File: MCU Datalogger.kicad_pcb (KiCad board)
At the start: 2 copper layers, 51.4 x 34.3 mm, 31 parts, among them J1 Conn_01x04_Male, J2 Conn_01x09_Male, J3 Conn_01x04_Male, J4 Conn_02x03_Odd_Even, U1 24LC1025, U2 DS1337S+, U3 24LC1025, U4 ATMEGA328P-AU, Y1 32.768 KHz, Y2 16 MHz

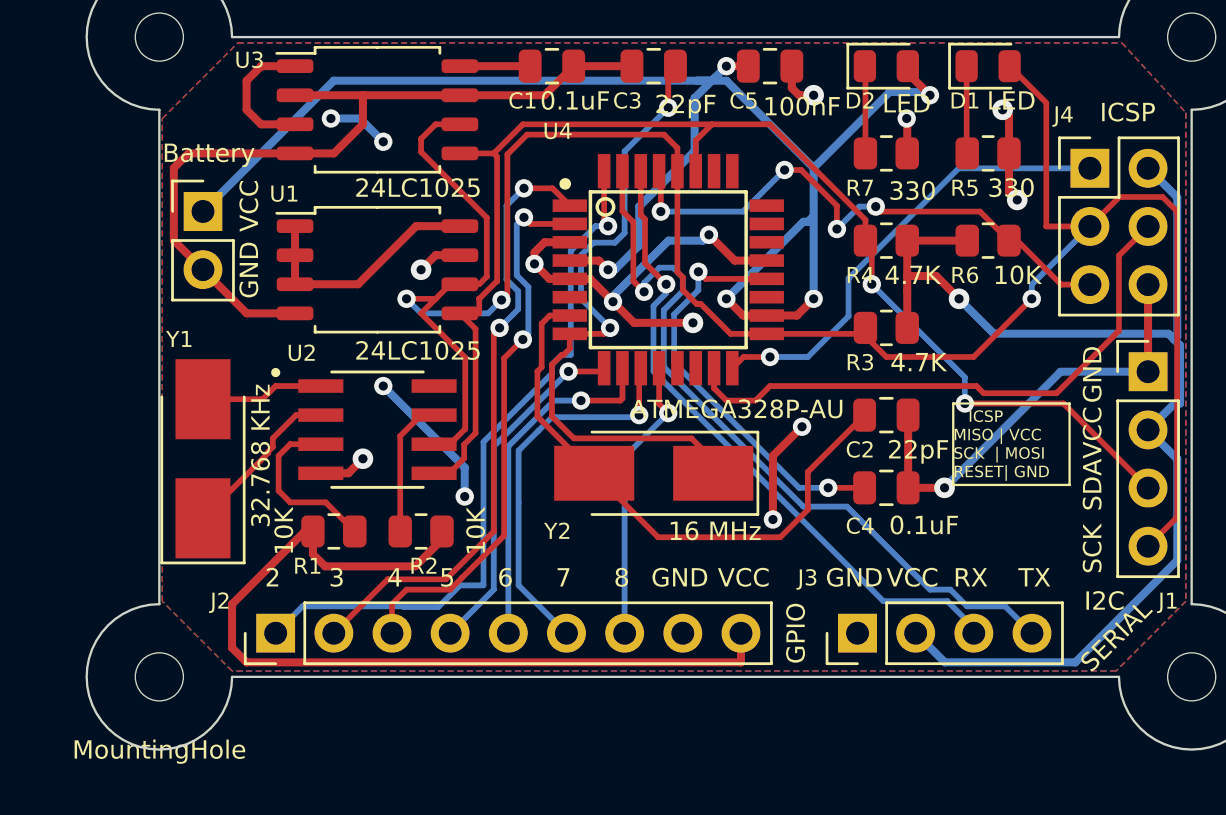
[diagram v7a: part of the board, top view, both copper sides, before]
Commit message: Completed 2-layer PCB project.
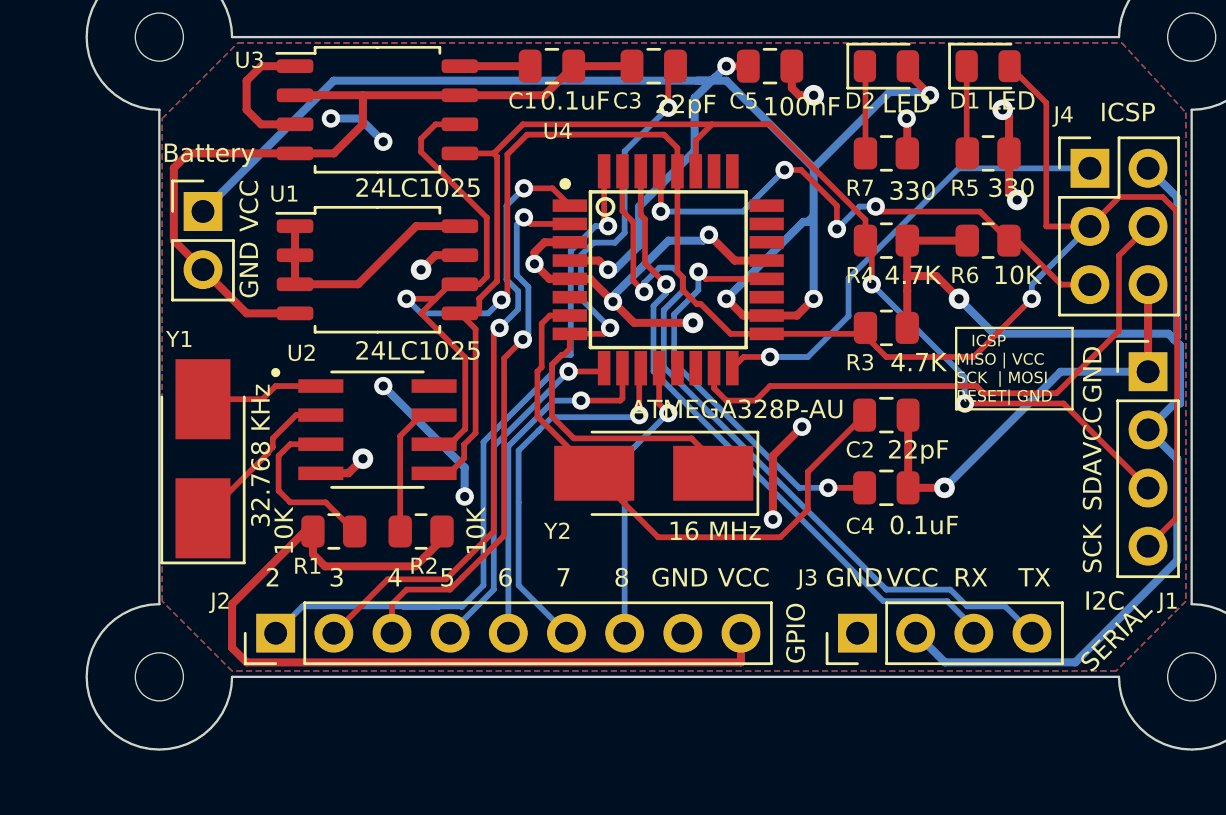
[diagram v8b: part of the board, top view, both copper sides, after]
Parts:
- renumbered G*** to G2, REF** to REF1
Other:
- board text added: "0.2000 mm / 0.0000 mm"
- board text added: "0.3000 mm"
- board text added: "1.6000 mm"
- board text added: "51.7350 mm x 34.5900 mm"
- board text added: "BOARD CHARACTERISTICS"
- board text added: "Board Thickness:"
- board text added: "Board overall dimensions:"
- board text added: "Castellated pads:"
- board text added: "Copper Finish:"
- board text added: "Copper Layer Count:"
- board text added: "Impedance Control:"
- board text added: "Min hole diameter:"
- board text added: "Min track/spacing:"
- board text added: "No"
- board text added: "None"
- board text added: "Plated Board Edge:"
